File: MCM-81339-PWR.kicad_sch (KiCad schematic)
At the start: 22 parts, among them J10 694108301002, U1 AZ1117CR-3.3TRG1, U2 LMR16006YQ

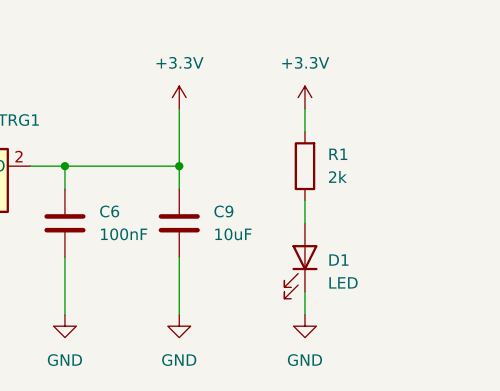
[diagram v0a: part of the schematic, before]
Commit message: add protection on uart, add fab outputs
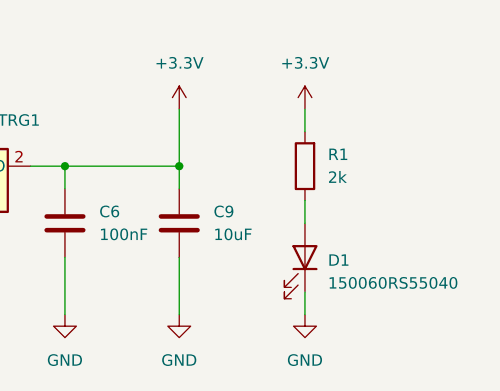
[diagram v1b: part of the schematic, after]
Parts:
- D1: value LED -> 150060RS55040
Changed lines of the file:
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@@
       (effects (font (size 1.27 1.27)) (justify left))
     )
-    (property "Value" "LED" (id 1) (at 265.43 98.1074 90)
+    (property "Value" "150060RS55040" (id 1) (at 265.43 98.1074 90)
       (effects (font (size 1.27 1.27)) (justify left))
     )
